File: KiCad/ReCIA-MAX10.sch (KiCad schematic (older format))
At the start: 15 parts, among them J1 Conn_02x03_Odd_Even, U1 AMS1117-3.3, U2 10M02SCU169, U3 SN74CBT16210, U4 SN74CBT16210, U5 8520_DIP_SOCKET

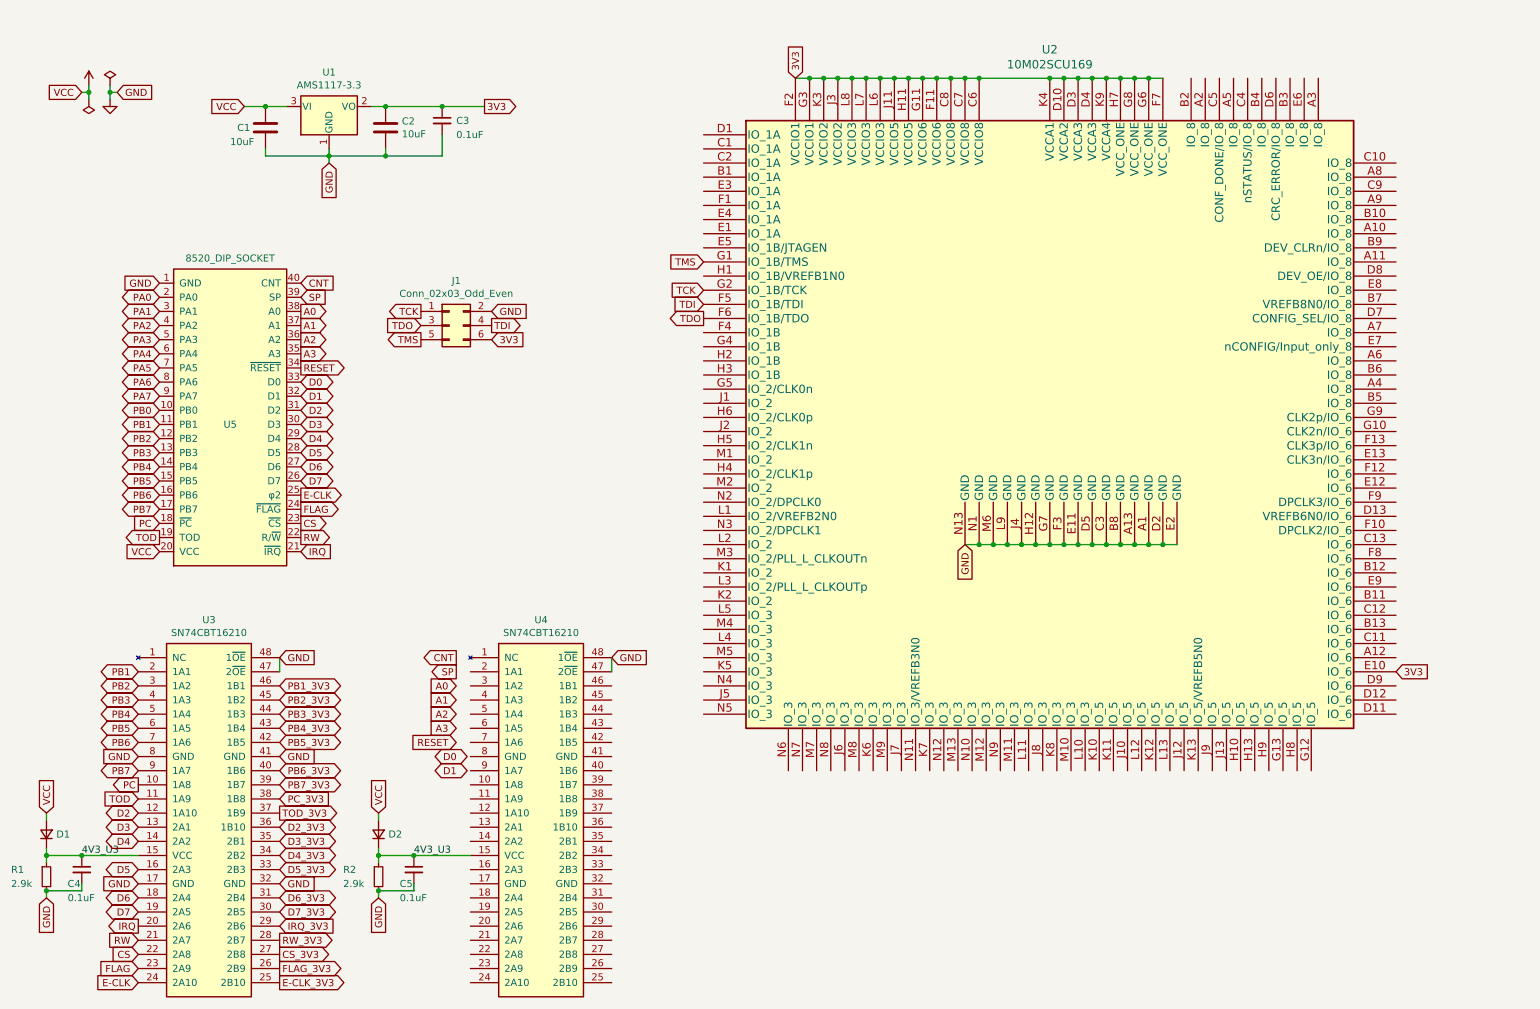
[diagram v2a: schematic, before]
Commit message: more routing and pin assignment
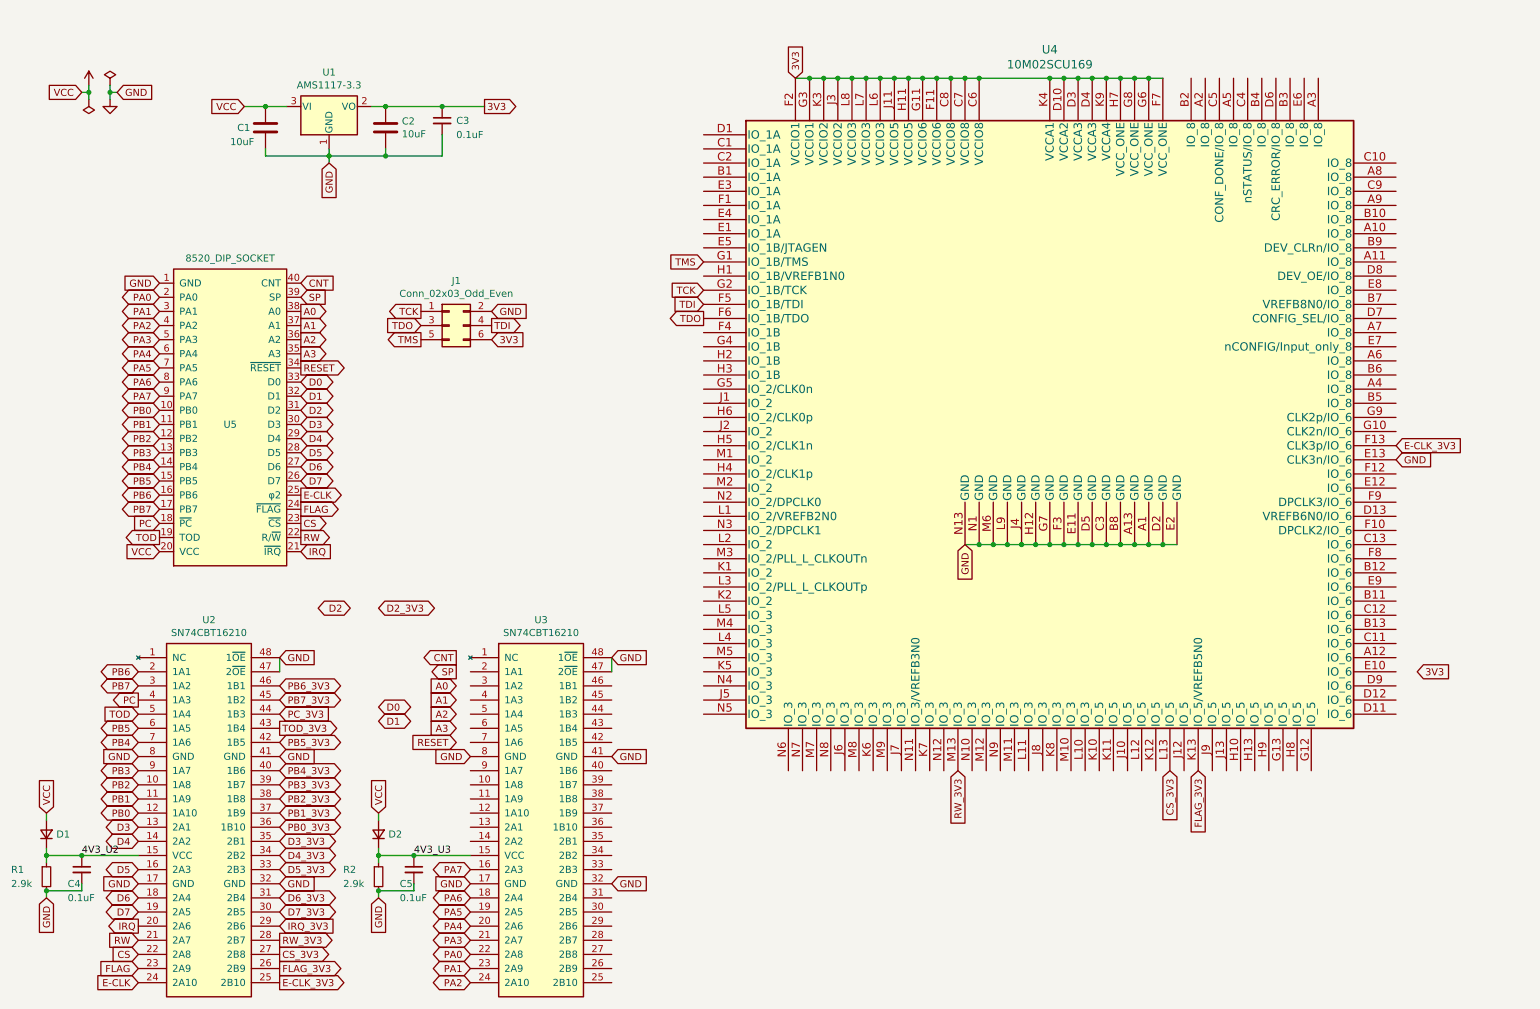
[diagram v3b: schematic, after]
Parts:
- renumbered U3 to U2, U4 to U3, U2 to U4
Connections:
- net 3V3: no longer U4.E10 (IO_6)
- net 4V3_U3: no longer C4.1, D1.1 (K), R1.1, U2.15 (VCC)
- net CS_3V3: now also U4.L13 (IO_5)
- net D2: no longer U2.12 (1A10)
- net D2_3V3: no longer U2.36 (1B10)
- net E-CLK_3V3: now also U4.F13 (CLK3p/IO_6)
- net FLAG_3V3: now also U4.K13 (IO_5/VREFB5N0)
- net GND: now also U3.17 (GND), U3.32 (GND), U3.41 (GND), U3.8 (GND), U4.E13 (CLK3n/IO_6)
- net PA0: now also U3.22 (2A8)
- net PA1: now also U3.23 (2A9)
- net PA2: now also U3.24 (2A10)
- net PA3: now also U3.21 (2A7)
- net PA4: now also U3.20 (2A6)
- net PA5: now also U3.19 (2A5)
- net PA6: now also U3.18 (2A4)
- net PA7: now also U3.16 (2A3)
- net PB0: now also U2.12 (1A10)
- net PB1: now also U2.11 (1A9); no longer U2.2 (1A1)
- net PB1_3V3: now also U2.37 (1B9); no longer U2.46 (1B1)
- net PB2: now also U2.10 (1A8); no longer U2.3 (1A2)
- net PB2_3V3: now also U2.38 (1B8); no longer U2.45 (1B2)
- net PB3: now also U2.9 (1A7); no longer U2.4 (1A3)
- net PB3_3V3: now also U2.39 (1B7); no longer U2.44 (1B3)
- net PB4: now also U2.7 (1A6); no longer U2.5 (1A4)
- net PB4_3V3: now also U2.40 (1B6); no longer U2.43 (1B4)
- net PB6: now also U2.2 (1A1); no longer U2.7 (1A6)
- net PB6_3V3: now also U2.46 (1B1); no longer U2.40 (1B6)
- net PB7: now also U2.3 (1A2); no longer U2.9 (1A7)
- net PB7_3V3: now also U2.45 (1B2); no longer U2.39 (1B7)
- net PC: now also U2.4 (1A3); no longer U2.10 (1A8)
- net PC_3V3: now also U2.44 (1B3); no longer U2.38 (1B8)
- net RW_3V3: now also U4.M13 (IO_3)
- net TOD: now also U2.5 (1A4); no longer U2.11 (1A9)
- net TOD_3V3: now also U2.43 (1B4); no longer U2.37 (1B9)
- new net 4V3_U2: C4.1, D1.1 (K), R1.1, U2.15 (VCC)
- new net PB0_3V3: U2.36 (1B10)
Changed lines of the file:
@@
 Connection ~ 3150 1600
 $Comp
-L ReCIA:10M02SCU169 U2
+L ReCIA:10M02SCU169 U4
 U 1 1 66C35F6F
 P 7850 3500
-F 0 "U2" H 7850 6153 60  0000 C CNN
+F 0 "U4" H 7850 6153 60  0000 C CNN
 F 1 "10M02SCU169" H 7850 6047 60  0000 C CNN
 F 2 "ReCIA:BGA-169_11.0x11.0mm_Layout13x13_P0.8mm_Ball0.5mm_Pad0.35mm_NSMD" H 7850 3850 60  0001 C CNN
@@
 Wire Wire Line
 	8550 1050 8650 1050
-Text GLabel 10300 5250 2    50   Input ~ 0
+Text GLabel 10450 5250 2    50   Input ~ 0
 3V3
 $Comp
-L ReCIA:SN74CBT16210 U3
+L ReCIA:SN74CBT16210 U2
 U 1 1 66D14302
 P 1900 6250
-F 0 "U3" H 1900 7617 50  0000 C CNN
+F 0 "U2" H 1900 7617 50  0000 C CNN
 F 1 "SN74CBT16210" H 1900 7526 50  0000 C CNN
 F 2 "Package_SO:TSSOP-48_4.4x9.7mm_P0.4mm" H 3550 6700 50  0001 C CNN
@@
 D5_3V3
 Text Label 1000 6550 0    50   ~ 0
-4V3_U3
+4V3_U2
 Text GLabel 2400 6550 2    50   BiDi ~ 0
 D4_3V3
 Text GLabel 2400 6450 2    50   BiDi ~ 0
 D3_3V3
-Text GLabel 1400 6250 0    50   BiDi ~ 0
-D2
-Text GLabel 2400 6350 2    50   BiDi ~ 0
-D2_3V3
 Text GLabel 3650 5650 0    50   Input ~ 0
 A3
@@
 Text GLabel 2550 3100 2    50   Output ~ 0
 RESET
-Text GLabel 3500 5850 2    50   BiDi ~ 0
+Text GLabel 3100 5500 2    50   BiDi ~ 0
 D0
-Text GLabel 3500 5950 2    50   BiDi ~ 0
+Text GLabel 3100 5600 2    50   BiDi ~ 0
 D1
 Text GLabel 2550 3000 2    50   Output ~ 0
@@
 Text GLabel 2550 2500 2    50   Input ~ 0
 CNT
-Text GLabel 1400 6150 0    50   Input ~ 0
-TOD
-Text GLabel 1400 6050 0    50   Output ~ 0
-PC
-Text GLabel 2400 6250 2    50   Output ~ 0
+Text GLabel 2400 5650 2    50   Output ~ 0
 TOD_3V3
-Text GLabel 2400 6150 2    50   Input ~ 0
+Text GLabel 2400 5550 2    50   Input ~ 0
 PC_3V3
-Text GLabel 1400 5250 0    50   BiDi ~ 0
-PB1
-Text GLabel 1400 5350 0    50   BiDi ~ 0
-PB2
-Text GLabel 1400 5450 0    50   BiDi ~ 0
-PB3
-Text GLabel 1400 5550 0    50   BiDi ~ 0
-PB4
-Text GLabel 1400 5650 0    50   BiDi ~ 0
-PB5
-Text GLabel 1400 5750 0    50   BiDi ~ 0
-PB6
-Text GLabel 1400 5950 0    50   BiDi ~ 0
-PB7
-Text GLabel 2400 6050 2    50   BiDi ~ 0
+Text GLabel 2400 5450 2    50   BiDi ~ 0
 PB7_3V3
-Text GLabel 2400 5950 2    50   BiDi ~ 0
+Text GLabel 2400 5350 2    50   BiDi ~ 0
 PB6_3V3
-Text GLabel 2400 5350 2    50   BiDi ~ 0
-PB1_3V3
-Text GLabel 2400 5450 2    50   BiDi ~ 0
-PB2_3V3
-Text GLabel 2400 5550 2    50   BiDi ~ 0
-PB3_3V3
-Text GLabel 2400 5650 2    50   BiDi ~ 0
-PB4_3V3
-Text GLabel 2400 5750 2    50   BiDi ~ 0
-PB5_3V3
-$Comp
-L ReCIA:SN74CBT16210 U4
+$Comp
+L ReCIA:SN74CBT16210 U3
 U 1 1 66E12D1D
 P 4250 6250
-F 0 "U4" H 4250 7617 50  0000 C CNN
+F 0 "U3" H 4250 7617 50  0000 C CNN
 F 1 "SN74CBT16210" H 4250 7526 50  0000 C CNN
 F 2 "Package_SO:TSSOP-48_4.4x9.7mm_P0.4mm" H 5900 6700 50  0001 C CNN
@@
 Text GLabel 3900 2900 2    50   Input ~ 0
 3V3
+Text GLabel 3750 7450 0    50   BiDi ~ 0
+PA2
+Text GLabel 3750 7350 0    50   BiDi ~ 0
+PA1
+Text GLabel 3750 7250 0    50   BiDi ~ 0
+PA0
+Text GLabel 3750 7150 0    50   BiDi ~ 0
+PA3
+Text GLabel 3750 7050 0    50   BiDi ~ 0
+PA4
+Text GLabel 3750 6950 0    50   BiDi ~ 0
+PA5
+Text GLabel 3750 6850 0    50   BiDi ~ 0
+PA6
+Text GLabel 3750 6650 0    50   BiDi ~ 0
+PA7
+Text GLabel 3750 6750 0    50   Input ~ 0
+GND
+Text GLabel 4750 6750 2    50   Input ~ 0
+GND
+Text GLabel 4750 5850 2    50   Input ~ 0
+GND
+Text GLabel 3750 5850 0    50   Input ~ 0
+GND
+Text GLabel 1400 5350 0    50   BiDi ~ 0
+PB7
+Text GLabel 1400 5250 0    50   BiDi ~ 0
+PB6
+Text GLabel 1400 5450 0    50   Output ~ 0
+PC
+Text GLabel 1400 5550 0    50   Input ~ 0
+TOD
+Text GLabel 1400 5650 0    50   BiDi ~ 0
+PB5
+Text GLabel 2400 5750 2    50   BiDi ~ 0
+PB5_3V3
+Text GLabel 1400 5750 0    50   BiDi ~ 0
+PB4
+Text GLabel 2400 5950 2    50   BiDi ~ 0
+PB4_3V3
+Text GLabel 2400 6050 2    50   BiDi ~ 0
+PB3_3V3
+Text GLabel 2400 6150 2    50   BiDi ~ 0
+PB2_3V3
+Text GLabel 2400 6250 2    50   BiDi ~ 0
+PB1_3V3
+Text GLabel 1400 5950 0    50   BiDi ~ 0
+PB3
+Text GLabel 1400 6050 0    50   BiDi ~ 0
+PB2
+Text GLabel 1400 6150 0    50   BiDi ~ 0
+PB1
+Text GLabel 2900 4800 0    50   BiDi ~ 0
+D2
+Text GLabel 3100 4800 2    50   BiDi ~ 0
+D2_3V3
+Text GLabel 1400 6250 0    50   BiDi ~ 0
+PB0
+Text GLabel 2400 6350 2    50   BiDi ~ 0
+PB0_3V3
+Text GLabel 10300 3650 2    50   Input ~ 0
+E-CLK_3V3
+Text GLabel 10300 3750 2    50   Input ~ 0
+GND
+Text GLabel 8900 5950 3    50   Input ~ 0
+FLAG_3V3
+Text GLabel 8700 5950 3    50   Input ~ 0
+CS_3V3
+Text GLabel 7200 5950 3    50   Input ~ 0
+RW_3V3
 $EndSCHEMATC

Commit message: more routing and pin assignment
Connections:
- net D3_3V3: now also U4.N8 (IO_3)
- net D4_3V3: now also U4.N9 (IO_3)
- net D5_3V3: now also U4.N10 (IO_3)
- net D6_3V3: now also U4.N11 (IO_3/VREFB3N0)
- net D7_3V3: now also U4.N12 (IO_3)
- net IRQ_3V3: now also U4.M11 (IO_3)
- net PB0_3V3: now also U4.N7 (IO_3)
- net PB1_3V3: now also U4.N6 (IO_3)
- net PB2_3V3: now also U4.N5 (IO_3)
- net PB3_3V3: now also U4.M5 (IO_3)
- net PB4_3V3: now also U4.M4 (IO_3)
- net PB5_3V3: now also U4.N4 (IO_3)
- net PB6_3V3: now also U4.N2 (IO_2/DPCLK0)
- net PB7_3V3: now also U4.N3 (IO_2/DPCLK1)
- net PC_3V3: now also U4.M1 (IO_2)
- net TOD_3V3: now also U4.H6 (IO_2/CLK0p)
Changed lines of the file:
@@
 Text GLabel 7200 5950 3    50   Input ~ 0
 RW_3V3
+Text GLabel 7600 5950 3    50   Output ~ 0
+IRQ_3V3
+Text GLabel 7100 5950 3    50   BiDi ~ 0
+D7_3V3
+Text GLabel 6900 5950 3    50   BiDi ~ 0
+D6_3V3
+Text GLabel 7300 5950 3    50   BiDi ~ 0
+D5_3V3
+Text GLabel 7500 5950 3    50   BiDi ~ 0
+D4_3V3
+Text GLabel 6300 5950 3    50   BiDi ~ 0
+D3_3V3
+Text GLabel 5400 4950 0    50   BiDi ~ 0
+PB4_3V3
+Text GLabel 5400 5150 0    50   BiDi ~ 0
+PB3_3V3
+Text GLabel 5400 5550 0    50   BiDi ~ 0
+PB2_3V3
+Text GLabel 6000 5950 3    50   BiDi ~ 0
+PB1_3V3
+Text GLabel 6100 5950 3    50   BiDi ~ 0
+PB0_3V3
+Text GLabel 5400 5350 0    50   BiDi ~ 0
+PB5_3V3
+Text GLabel 5400 4250 0    50   BiDi ~ 0
+PB7_3V3
+Text GLabel 5400 4050 0    50   BiDi ~ 0
+PB6_3V3
+Text GLabel 5400 3750 0    50   Output ~ 0
+PC_3V3
+Text GLabel 5400 3450 0    50   Input ~ 0
+TOD_3V3
 $EndSCHEMATC

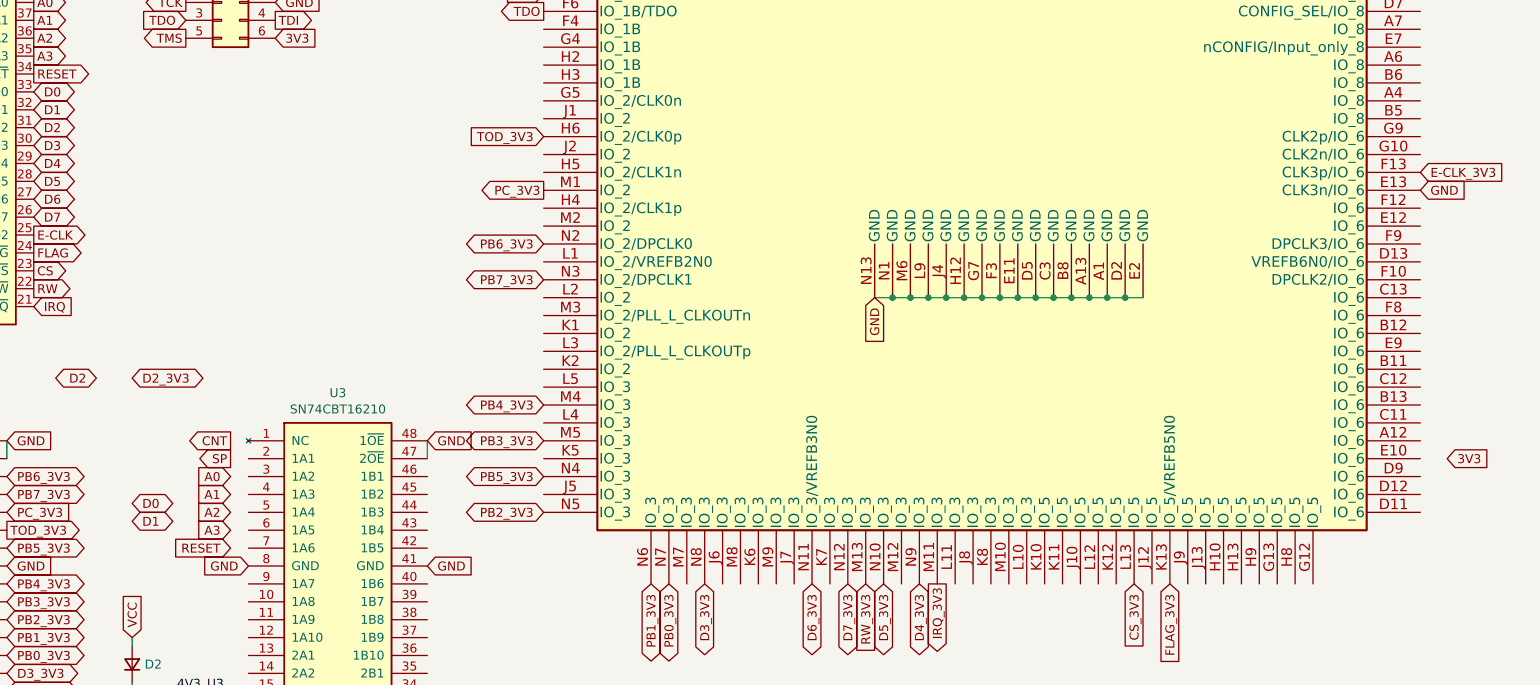
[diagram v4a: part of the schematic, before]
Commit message: routing JTAG plus more routing of power to BGA chip
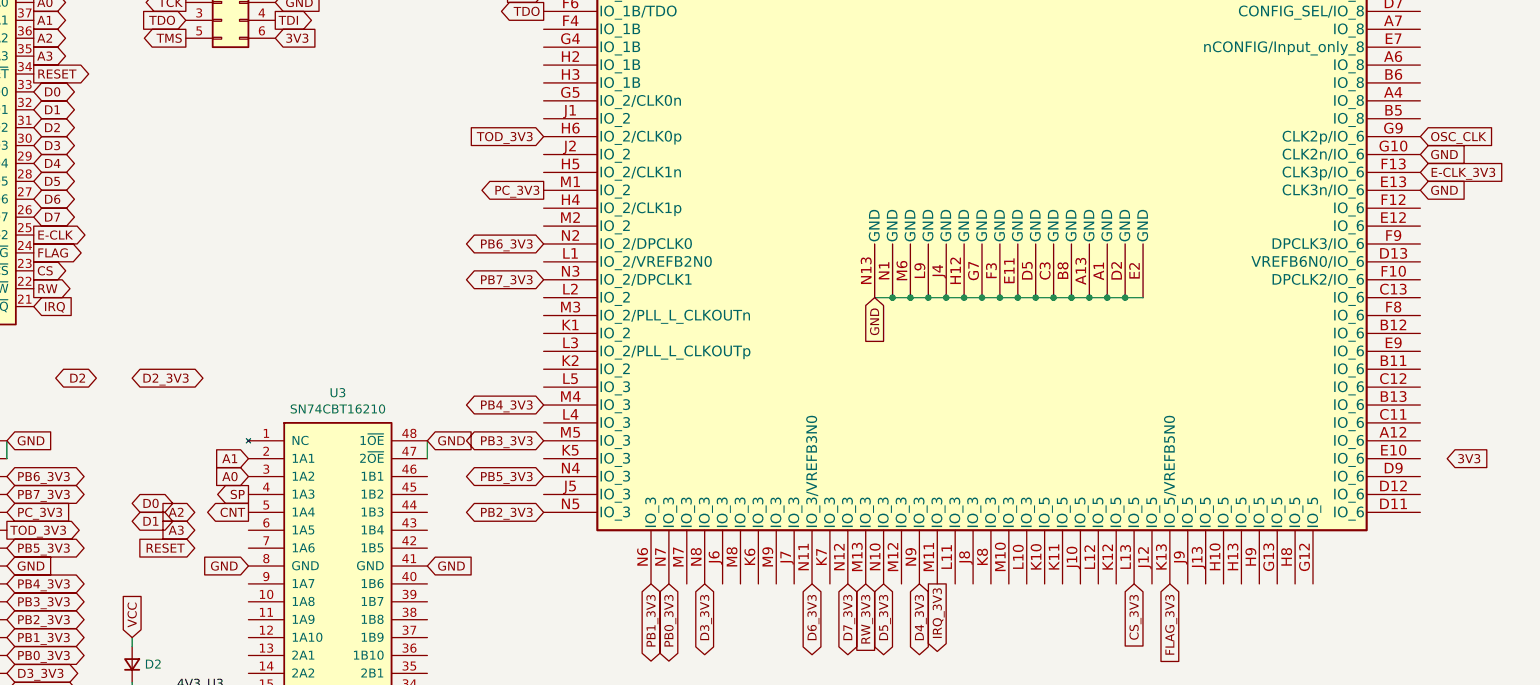
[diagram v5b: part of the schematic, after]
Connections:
- net A0: now also U3.3 (1A2)
- net A1: now also U3.2 (1A1)
- net CNT: now also U3.5 (1A4)
- net GND: now also U4.G10 (CLK2n/IO_6)
- net SP: now also U3.4 (1A3)
- net OSC_CLK: now reaches U4.G9 (CLK2p/IO_6)
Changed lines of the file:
@@
 Text GLabel 1550 4100 0    50   BiDi ~ 0
 PB7
-Text GLabel 3650 5350 0    50   Input ~ 0
+Text GLabel 3750 5350 0    50   Input ~ 0
 A0
-Text GLabel 3650 5450 0    50   Input ~ 0
+Text GLabel 3750 5250 0    50   Input ~ 0
 A1
-Text GLabel 3650 5550 0    50   Input ~ 0
+Text GLabel 3450 5550 0    50   Input ~ 0
 A2
 Text GLabel 2550 3200 2    50   BiDi ~ 0
@@
 Text GLabel 2550 4300 2    50   Output ~ 0
 RW
-Text GLabel 3650 5150 0    50   Output ~ 0
+Text GLabel 3750 5550 0    50   Output ~ 0
 CNT
-Text GLabel 3650 5250 0    50   Output ~ 0
+Text GLabel 3750 5450 0    50   Output ~ 0
 SP
 $Comp
@@
 Text GLabel 2400 6450 2    50   BiDi ~ 0
 D3_3V3
-Text GLabel 3650 5650 0    50   Input ~ 0
+Text GLabel 3450 5650 0    50   Input ~ 0
 A3
-Text GLabel 3650 5750 0    50   Input ~ 0
+Text GLabel 3450 5750 0    50   Input ~ 0
 RESET
 Text GLabel 2550 3100 2    50   Output ~ 0
@@
 Text GLabel 5400 3450 0    50   Input ~ 0
 TOD_3V3
+Text GLabel 10300 3450 2    50   Input ~ 0
+OSC_CLK
+Text GLabel 10300 3550 2    50   Input ~ 0
+GND
 $EndSCHEMATC
